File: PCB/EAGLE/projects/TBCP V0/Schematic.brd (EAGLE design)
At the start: 160.6 x 99.4 mm, 76 parts, among them IC1 LM7805_TO220V, J1 12 Supply, J2 TB Header, J3 FP Header, U1 ESP32-DEVKITC, U2 TLE9201SG

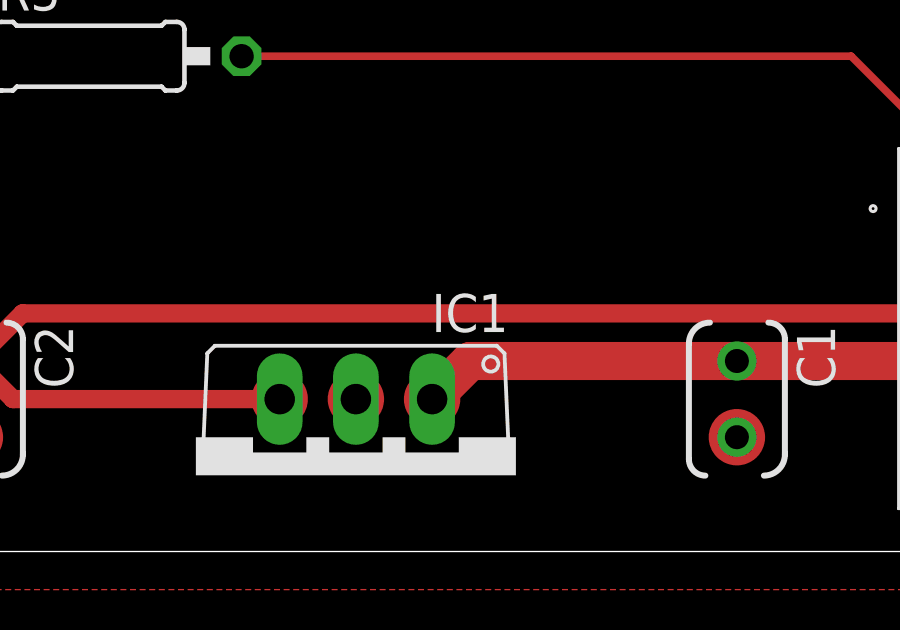
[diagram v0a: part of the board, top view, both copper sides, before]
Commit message: Name change
Updated IC1 to U3
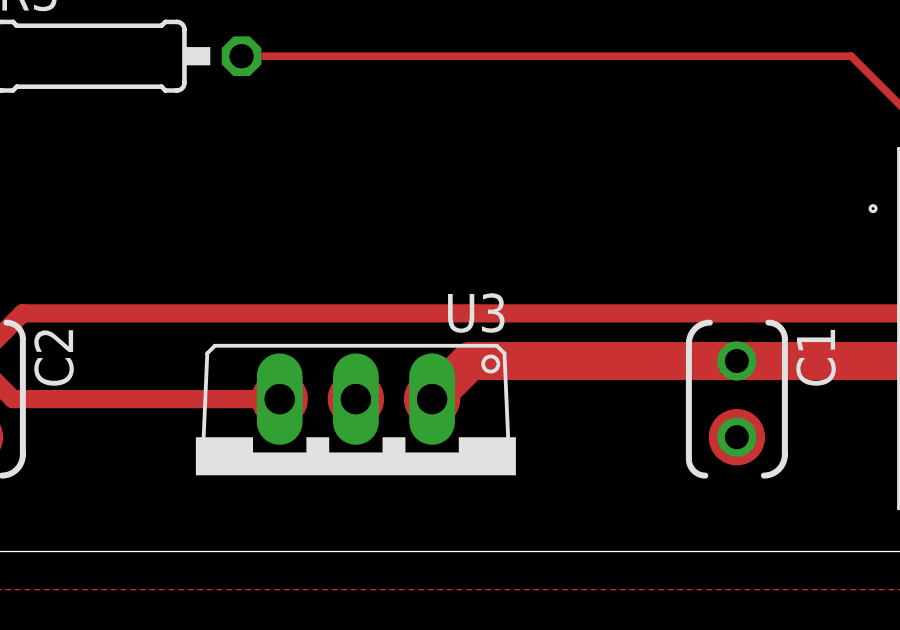
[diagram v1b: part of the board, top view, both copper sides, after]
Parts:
- renumbered IC1 to U3
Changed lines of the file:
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@@
 <attribute name="NAME" x="18.415" y="67.31" size="1.016" layer="25" ratio="18"/>
 </element>
-<element name="IC1" library="IC_Power-Management" library_urn="urn:adsk.eagle:library:16378392" package="TO220V" package3d_urn="urn:adsk.eagle:package:16417/2" value="LM7805_TO220V" x="83.82" y="2.54" smashed="yes" rot="R180">
+<element name="U3" library="IC_Power-Management" library_urn="urn:adsk.eagle:library:16378392" package="TO220V" package3d_urn="urn:adsk.eagle:package:16417/2" value="LM7805_TO220V" x="83.82" y="2.54" smashed="yes" rot="R180">
 <attribute name="CATEGORY" value="IC_Linear" x="33.02" y="86.36" size="1.778" layer="27" rot="R180" display="off"/>
 <attribute name="DESCRIPTION" value="5V Voltage Regulator" x="33.02" y="86.36" size="1.778" layer="27" rot="R180" display="off"/>
@@
 <contactref element="R4" pad="1"/>
 <contactref element="R6" pad="1"/>
-<contactref element="IC1" pad="2"/>
+<contactref element="U3" pad="2"/>
 <contactref element="C1" pad="2"/>
 <contactref element="C2" pad="2"/>
@@
 </signal>
 <signal name="12VDC">
-<contactref element="IC1" pad="1"/>
+<contactref element="U3" pad="1"/>
 <contactref element="C1" pad="1"/>
 <contactref element="C3" pad="+"/>
@@
 <contactref element="E8" pad="PAD"/>
 <contactref element="E55" pad="PAD"/>
-<contactref element="IC1" pad="3"/>
+<contactref element="U3" pad="3"/>
 <contactref element="C2" pad="1"/>
 <contactref element="U1" pad="19"/>
